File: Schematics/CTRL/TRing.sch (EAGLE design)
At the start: 39 parts

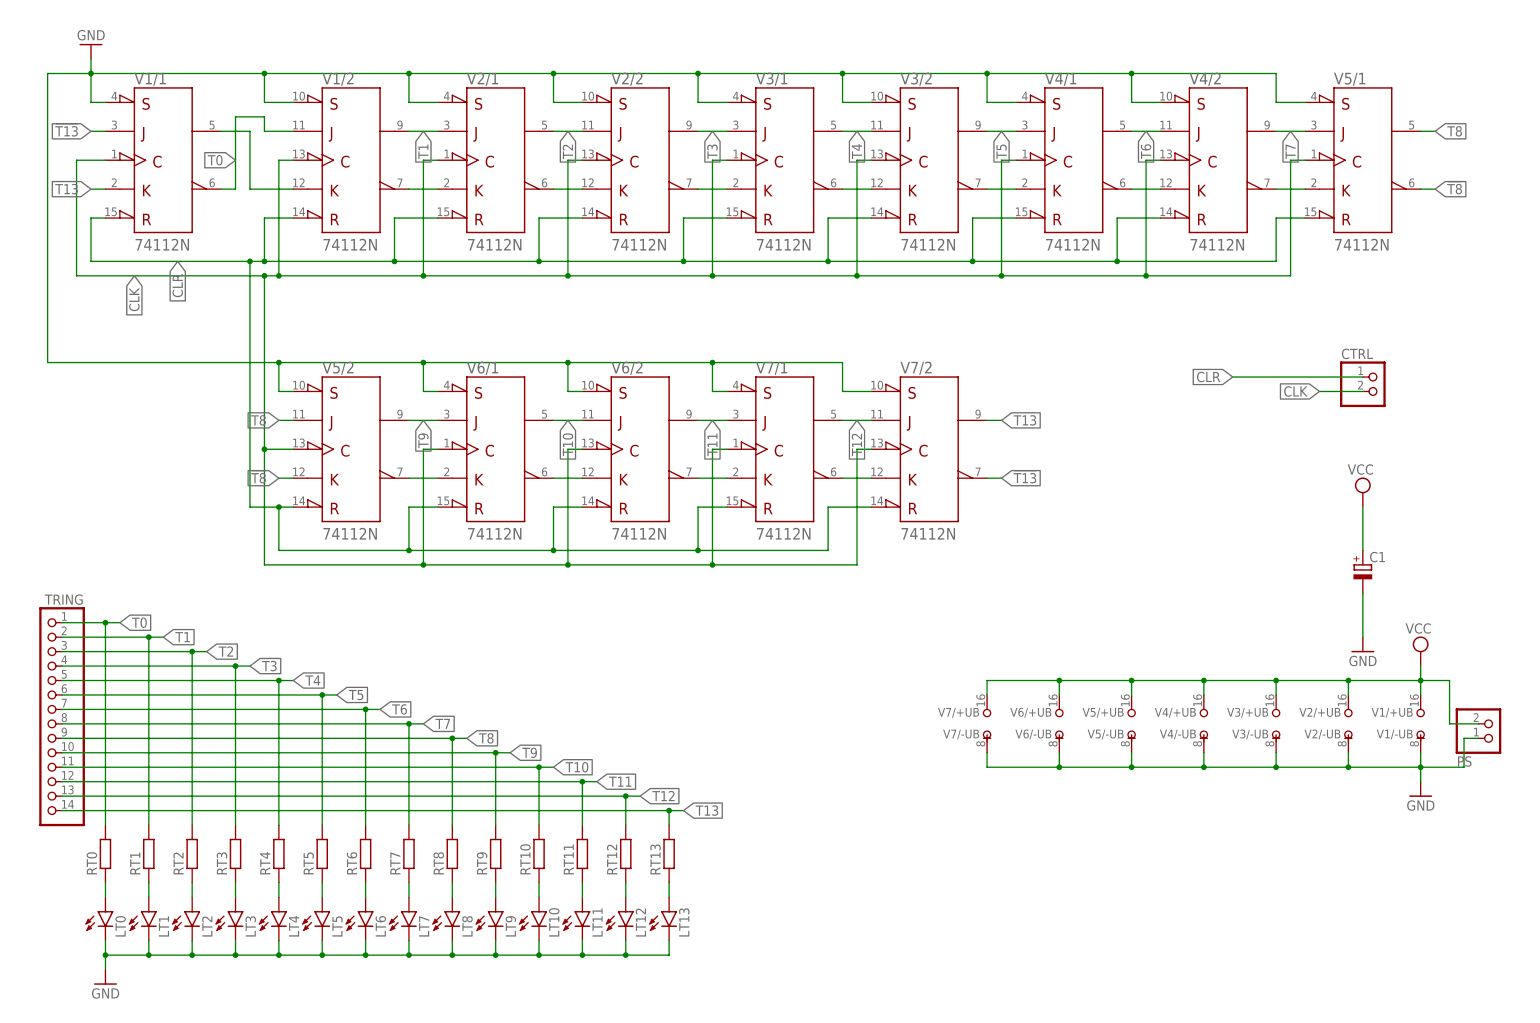
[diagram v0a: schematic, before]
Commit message: Reduce Tring width
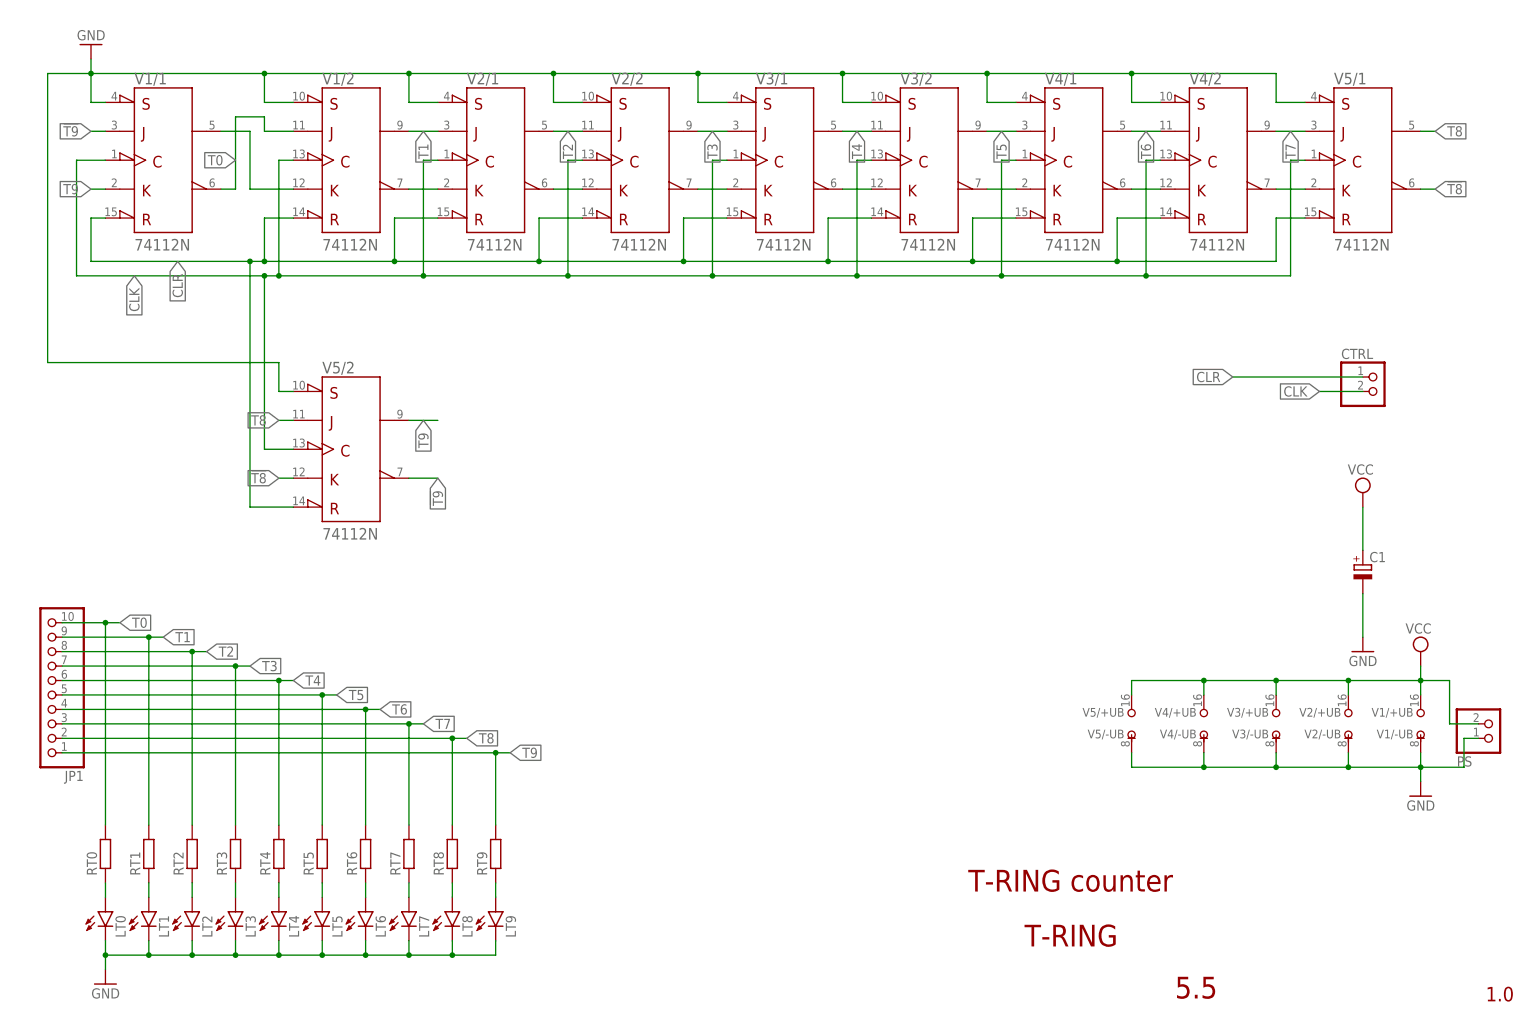
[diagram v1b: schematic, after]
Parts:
- removed LT10, LT11, LT12, LT13: (no value), led:LED5MM
- removed RT10, RT11, RT12, RT13: (no value), rcl:R-EU_0204/7
- removed TRING: (no value), pinhead:PINHD-1X14
- removed V6, V7: 74112N, 74ttl-din:74112N
- added JP1: (no value), pinhead:PINHD-1X10
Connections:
- removed net !T13: V1/1.J, V7/2.!Q
- removed net N$12: V5/2.!Q, V6/1.K
- removed net N$14: V6/1.!Q, V6/2.K
- removed net N$20: LT10.A, RT10.1
- removed net N$21: LT11.A, RT11.1
- removed net N$22: V6/2.!Q, V7/1.K
- removed net N$24: LT12.A, RT12.1
- removed net N$25: V7/1.!Q, V7/2.K
- removed net N$26: LT13.A, RT13.1
- removed net T10: RT10.2, TRING.11, V6/1.Q, V6/2.J
- removed net T11: RT11.2, TRING.12, V6/2.Q, V7/1.J
- removed net T12: RT12.2, TRING.13, V7/1.Q, V7/2.J
- removed net T13: RT13.2, TRING.14, V1/1.K, V7/2.Q
- new net !T9: V1/1.J, V5/2.!Q
- net CLK: no longer V6/1.CLK, V6/2.CLK, V7/1.CLK, V7/2.CLK
- net CLR: no longer V6/1.!CLR, V6/2.!CLR, V7/1.!CLR, V7/2.!CLR
- net GND: no longer LT10.C, LT11.C, LT12.C, LT13.C, V6/-UB.-UB, V6/1.!PRE, V6/2.!PRE, V7/-UB.-UB, V7/1.!PRE, V7/2.!PRE
- net T0: now also JP1.10; no longer TRING.1
- net T1: now also JP1.9; no longer TRING.2
- net T2: now also JP1.8; no longer TRING.3
- net T3: now also JP1.7; no longer TRING.4
- net T4: now also JP1.6; no longer TRING.5
- net T5: now also JP1.5; no longer TRING.6
- net T6: now also JP1.4; no longer TRING.7
- net T7: now also JP1.3; no longer TRING.8
- net T8: now also JP1.2; no longer TRING.9
- net T9: now also JP1.1, V1/1.K; no longer TRING.10, V6/1.J
- net VCC: no longer V6/+UB.+UB, V7/+UB.+UB
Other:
- note added: "1.0"
- note added: "5.5"
- note added: "T-RING"
- note added: "T-RING counter"

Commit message: Changed order of LEDs and widht is now 11bits (0-10).
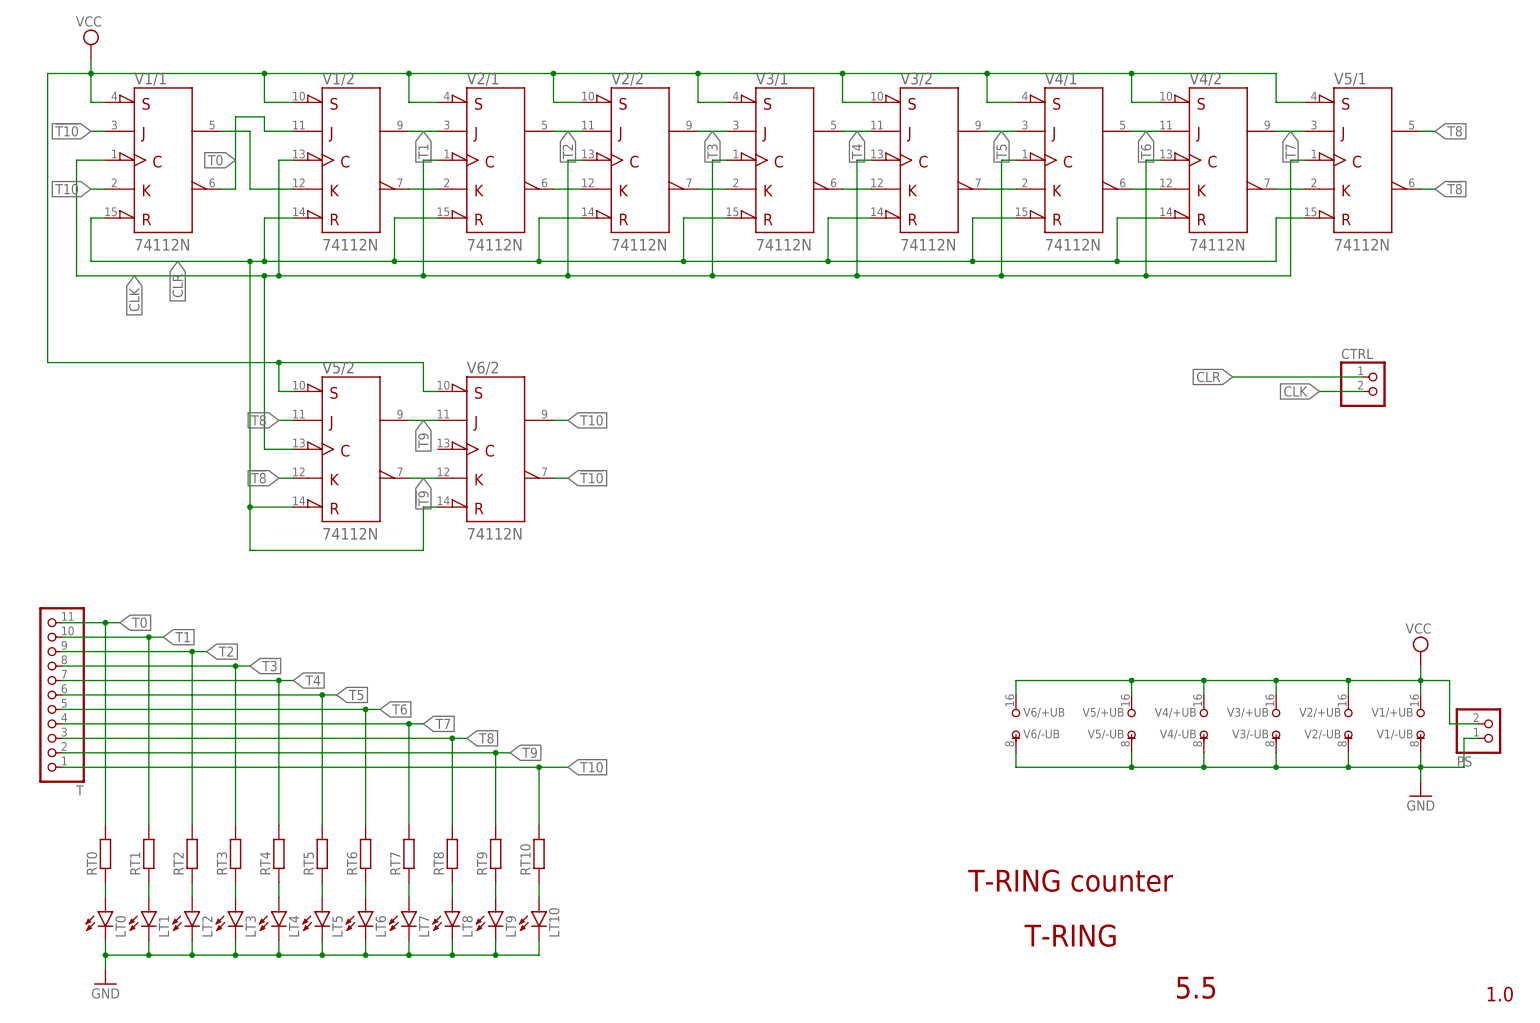
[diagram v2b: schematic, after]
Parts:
- removed C1: (no value), rcl:CPOL-EUE2.5-6
- removed JP1: (no value), pinhead:PINHD-1X10
- added LT10: (no value), led:LED5MM
- added RT10: (no value), rcl:R-EU_0204/7
- added T: (no value), pinhead:PINHD-1X11
- added V6: 74112N, 74ttl-din:74112N
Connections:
- new net !T10: V1/1.J, V6/2.!Q
- new net N$12: LT10.A, RT10.1
- new net T10: RT10.2, T.1, V1/1.K, V6/2.Q
- net !T9: now also V6/2.K; no longer V1/1.J
- net CLR: now also V6/2.!CLR
- net GND: now also LT10.C, V6/-UB.-UB; no longer C1.-, V1/1.!PRE, V1/2.!PRE, V2/1.!PRE, V2/2.!PRE, V3/1.!PRE, V3/2.!PRE, V4/1.!PRE, V4/2.!PRE, V5/1.!PRE, V5/2.!PRE
- net T0: now also T.11; no longer JP1.10
- net T1: now also T.10; no longer JP1.9
- net T2: now also T.9; no longer JP1.8
- net T3: now also T.8; no longer JP1.7
- net T4: now also T.7; no longer JP1.6
- net T5: now also T.6; no longer JP1.5
- net T6: now also T.5; no longer JP1.4
- net T7: now also T.4; no longer JP1.3
- net T8: now also T.3; no longer JP1.2
- net T9: now also T.2, V6/2.J; no longer JP1.1, V1/1.K
- net VCC: now also V1/1.!PRE, V1/2.!PRE, V2/1.!PRE, V2/2.!PRE, V3/1.!PRE, V3/2.!PRE, V4/1.!PRE, V4/2.!PRE, V5/1.!PRE, V5/2.!PRE, V6/+UB.+UB, V6/2.!PRE; no longer C1.+

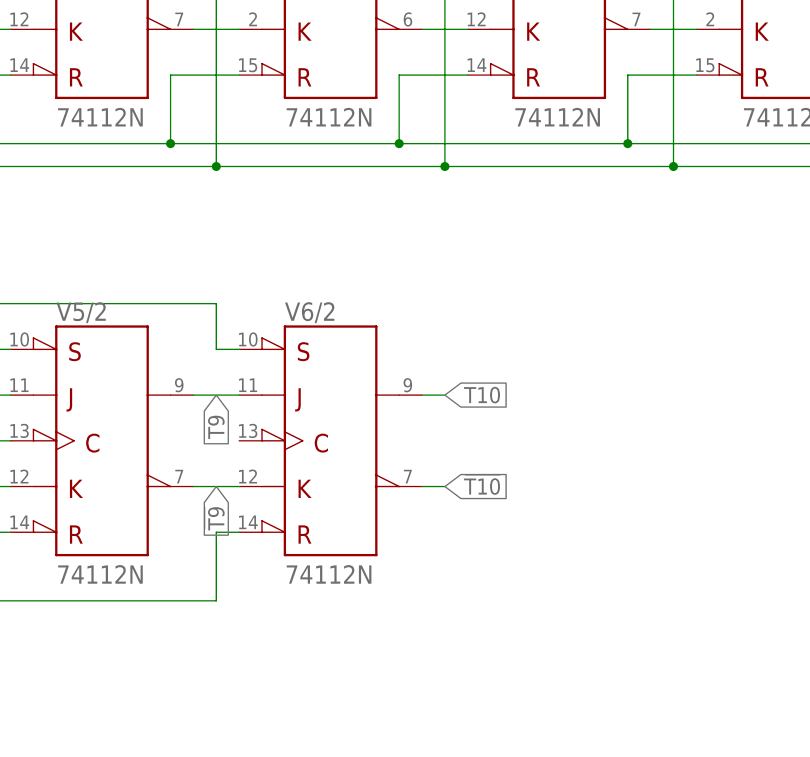
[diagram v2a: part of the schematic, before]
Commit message: Fixed 2 problems, that I found after ordering boards
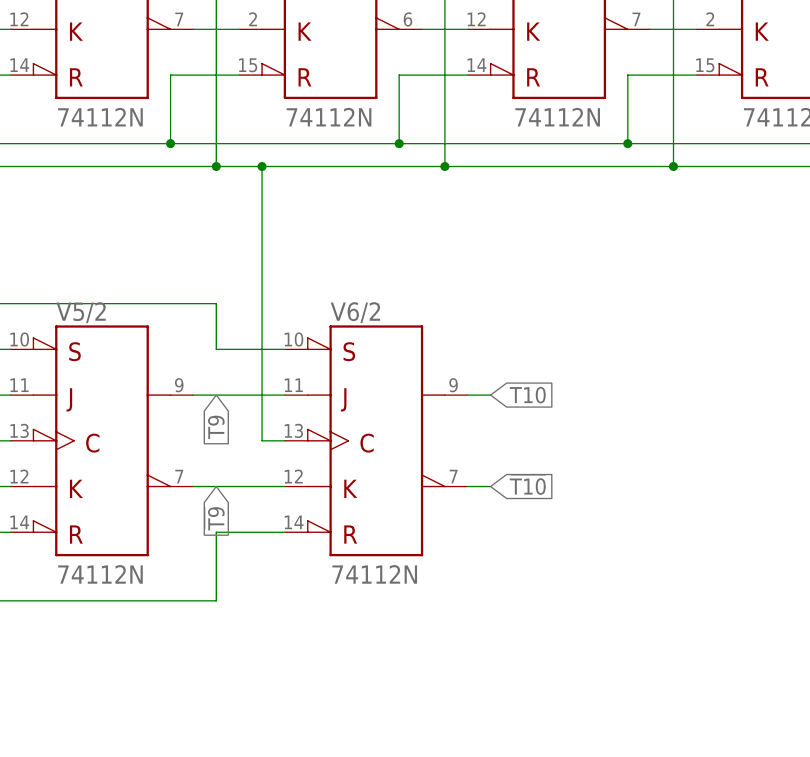
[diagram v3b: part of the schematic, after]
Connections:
- net CLK: now also V6/2.CLK
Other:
- moved on the sheet: V6/2
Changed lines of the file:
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@@
 <attribute name="VALUE" x="97.155" y="18.288" size="1.778" layer="96" rot="R90"/>
 </instance>
-<instance part="V6" gate="/2" x="83.82" y="104.14" smashed="yes">
-<attribute name="NAME" x="78.74" y="117.475" size="2.032" layer="95"/>
-<attribute name="VALUE" x="78.74" y="88.265" size="2.032" layer="96"/>
+<instance part="V6" gate="/2" x="88.9" y="104.14" smashed="yes">
+<attribute name="NAME" x="83.82" y="117.475" size="2.032" layer="95"/>
+<attribute name="VALUE" x="83.82" y="88.265" size="2.032" layer="96"/>
 </instance>
 <instance part="SUPPLY3" gate="G$1" x="12.7" y="175.26" smashed="yes" rot="MR0">
@@
 <wire x1="71.12" y1="86.36" x2="71.12" y2="93.98" width="0.1524" layer="91"/>
 <pinref part="V6" gate="/2" pin="!CLR"/>
-<wire x1="71.12" y1="93.98" x2="73.66" y2="93.98" width="0.1524" layer="91"/>
+<wire x1="71.12" y1="93.98" x2="78.74" y2="93.98" width="0.1524" layer="91"/>
 </segment>
 <segment>
@@
 <segment>
 <pinref part="V5" gate="/2" pin="Q"/>
-<wire x1="68.58" y1="109.22" x2="73.66" y2="109.22" width="0.1524" layer="91"/>
+<wire x1="68.58" y1="109.22" x2="78.74" y2="109.22" width="0.1524" layer="91"/>
 <label x="71.12" y="109.22" size="1.778" layer="95" rot="R270" xref="yes"/>
 <pinref part="V6" gate="/2" pin="J"/>
@@
 <segment>
 <pinref part="V5" gate="/2" pin="!Q"/>
-<wire x1="73.66" y1="99.06" x2="68.58" y2="99.06" width="0.1524" layer="91"/>
+<wire x1="78.74" y1="99.06" x2="68.58" y2="99.06" width="0.1524" layer="91"/>
 <label x="71.12" y="99.06" size="1.778" layer="95" rot="R270" xref="yes"/>
 <pinref part="V6" gate="/2" pin="K"/>
@@
 <pinref part="V2" gate="/1" pin="CLK"/>
 <wire x1="71.12" y1="154.94" x2="73.66" y2="154.94" width="0.1524" layer="91"/>
-<wire x1="71.12" y1="134.62" x2="96.52" y2="134.62" width="0.1524" layer="91"/>
+<wire x1="71.12" y1="134.62" x2="76.2" y2="134.62" width="0.1524" layer="91"/>
 <junction x="71.12" y="134.62"/>
+<wire x1="76.2" y1="134.62" x2="96.52" y2="134.62" width="0.1524" layer="91"/>
 <wire x1="96.52" y1="134.62" x2="96.52" y2="154.94" width="0.1524" layer="91"/>
 <pinref part="V2" gate="/2" pin="CLK"/>
@@
 <junction x="43.18" y="134.62"/>
 <label x="20.32" y="134.62" size="1.778" layer="95" rot="R270" xref="yes"/>
+<pinref part="V6" gate="/2" pin="CLK"/>
+<wire x1="78.74" y1="104.14" x2="76.2" y2="104.14" width="0.1524" layer="91"/>
+<wire x1="76.2" y1="104.14" x2="76.2" y2="134.62" width="0.1524" layer="91"/>
+<junction x="76.2" y="134.62"/>
 </segment>
 <segment>
@@
 <wire x1="71.12" y1="119.38" x2="71.12" y2="114.3" width="0.1524" layer="91"/>
 <pinref part="V6" gate="/2" pin="!PRE"/>
-<wire x1="71.12" y1="114.3" x2="73.66" y2="114.3" width="0.1524" layer="91"/>
+<wire x1="71.12" y1="114.3" x2="78.74" y2="114.3" width="0.1524" layer="91"/>
 <pinref part="SUPPLY3" gate="G$1" pin="VCC"/>
 </segment>
@@
 <segment>
 <pinref part="V6" gate="/2" pin="Q"/>
-<wire x1="96.52" y1="109.22" x2="93.98" y2="109.22" width="0.1524" layer="91"/>
-<label x="96.52" y="109.22" size="1.778" layer="95" xref="yes"/>
+<wire x1="101.6" y1="109.22" x2="99.06" y2="109.22" width="0.1524" layer="91"/>
+<label x="101.6" y="109.22" size="1.778" layer="95" xref="yes"/>
 </segment>
 <segment>
@@
 <segment>
 <pinref part="V6" gate="/2" pin="!Q"/>
-<wire x1="96.52" y1="99.06" x2="93.98" y2="99.06" width="0.1524" layer="91"/>
-<label x="96.52" y="99.06" size="1.778" layer="95" xref="yes"/>
-</segment>
-<segment>
+<wire x1="101.6" y1="99.06" x2="99.06" y2="99.06" width="0.1524" layer="91"/>
+<label x="101.6" y="99.06" size="1.778" layer="95" xref="yes"/>
+</segment>
+<segment>
